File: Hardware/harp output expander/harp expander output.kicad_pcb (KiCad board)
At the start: 2 copper layers, 124.5 x 80.4 mm, 167 parts, among them IC1 ATXMEGA128A1U-AU, IC10 SN74LVC1G125DBVT, IC2 USBLC6-2SC6, IC3 FT232RL-REEL, IC4 TLV70033DDCR, IC5 TLV70033DDCR, IC6 SI8621BC-B-ISR, IC7 SN74LVC1G125DBVT, IC8 SN74LVC1G125DBVT, IC9 SN74LVC1G125DBVT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

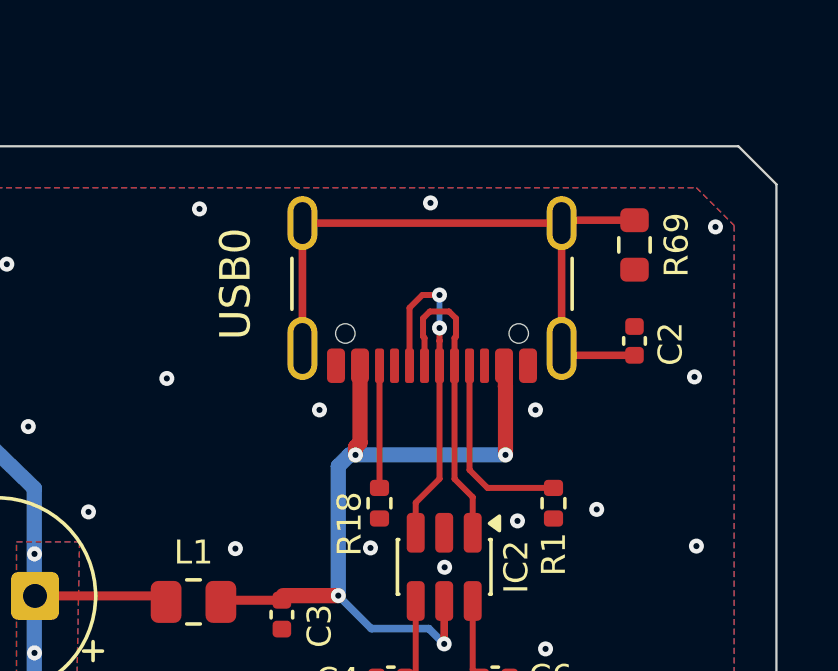
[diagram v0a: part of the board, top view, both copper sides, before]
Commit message: corrigida posição USB-C & gerados ficheiros de produção nos 3 projectos
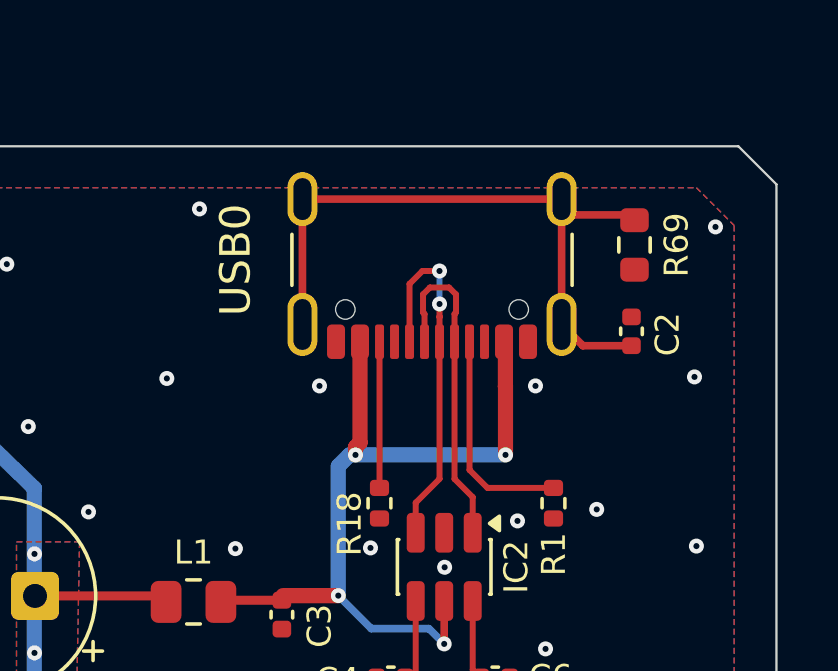
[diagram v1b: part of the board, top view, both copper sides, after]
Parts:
- moved USB0 0.80 mm to (199.3, 67.6)
- moved C2 0.34 mm to (205.9, 71.0)
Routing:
- net /5VUSB: track 25.6 -> 27.2 mm
- net Net-(IC2-I/O1-Pad1): track 9.89 -> 10.7 mm
- net Net-(USB0-CC2): track 4.07 -> 4.87 mm
- net Net-(USB0-CC1): track 6.52 -> 7.32 mm
- net Net-(IC2-I/O2-Pad3): track 10.9 -> 11.7 mm
- net Net-(USB0-SHIELD): track 22.0 -> 22.7 mm
- net GND: vias 420 -> 419
